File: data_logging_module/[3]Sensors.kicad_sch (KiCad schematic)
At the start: 4 parts, among them U3 BME280

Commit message: Initial scheme
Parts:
- added C301, C302, C303, C304: 100nF, Capacitor_SMD:C_0805_2012Metric, symbol Device:C
- added R301, R302, R303: 4k7R, Resistor_SMD:R_0805_2012Metric, symbol Device:R
- added R304, R305: 5k1R, Resistor_SMD:R_0805_2012Metric, symbol Device:R
- added U301: BME280, Package_LGA:Bosch_LGA-8_2.5x2.5mm_P0.65mm_ClockwisePinNumbering, symbol Sensor:BME280
- added U5: DS18B20, Package_TO_SOT_THT:TO-92_Inline, symbol Sensor_Temperature:DS18B20
- RLO300: renamed from R10; value LDR07 -> LDR
- renumbered C11 to C300, R11 to R300, U3 to U300
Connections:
- net +3.3V: now also U300.2 (CSB), U300.6 (VDDIO), C301.1, C303.1, R302.1, R303.1, R304.1, U301.6 (VDDIO); no longer RLO300.2
- net GND: now also U300.1 (GND), U300.7 (GND), C301.2, C302.2, C303.2, C304.2, R305.2, U301.1 (GND), U301.7 (GND), U5.1 (GND)
- net I2C_SDA: now reaches U300.3 (SDI)
- net I2C_SDA: now also R302.2
- net I2C_SCL: now reaches U300.4 (SCK)
- net I2C_SCL: now also R303.2
- net at U300.5 (SDO): now also R304.2, R305.1
- net +3.3VA: now reaches U300.8 (VDD)
- net +3.3VA: now also RLO300.2, C302.1, C304.1, R301.1, U301.8 (VDD), U5.3 (V_{DD})
- net LDR_IN renamed LDR
- new net BME280_SCB: U301.2 (CSB)
- new net BME280_SCK: U301.4 (SCK)
- new net BME280_SDI: U301.3 (SDI)
- new net BME280_SDO: U301.5 (SDO)
- new net DS18B20: R301.2, U5.2 (DQ)
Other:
- note added: "BME 280 I2C"
- note added: "BME 280 SPI"
- note added: "DS18B20"
- note added: "LRO"
- note added: "SDO: I2C address bit 0 GND: '0'; VDDIO: '1'"
- moved on the sheet: C300, R300, RLO300, U300

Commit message: BOM updates
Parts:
- C300: Manufacturer Part Number (none) -> CL10B104KB8NNNC
- C301, C302, C303, C304: footprint Capacitor_SMD:C_0805_2012Metric -> Capacitor_SMD:C_0603_1608Metric; Manufacturer Part Number (none) -> CL10B104KB8NNNC
- R300: Manufacturer Part Number (none) -> 0805W8F1002T5E
- R301, R302, R303: Manufacturer Part Number (none) -> 0805W8F4701T5E
- R304, R305: Manufacturer UNI-ROYAL(Uniroyal Elec) -> UNI-ROYAL(Uniroyal Elec); Manufacturer Part Number (none) -> 0805W8F5101T5E
- RLO300: Manufacturer Part Number (none) -> GL5528(10-20)
- U300, U301: Manufacturer (none) -> Bosch Sensortec; Manufacturer Part Number (none) -> BME280
- U5: Manufacturer (none) -> UMW(Youtai Semiconductor Co., Ltd.); Manufacturer Part Number (none) -> DS18B20(UMW)
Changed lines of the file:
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@@
 			)
 		)
-		(property "Footprint" "Capacitor_SMD:C_0805_2012Metric"
+		(property "Footprint" "Capacitor_SMD:C_0603_1608Metric"
 			(at 36.5252 96.52 0)
 			(effects
@@
 		)
 		(property "Manufacturer Product Number" "CL21A106KOQNNNE"
+			(at 35.56 92.71 0)
+			(effects
+				(font
+					(size 1.27 1.27)
+				)
+				(hide yes)
+			)
+		)
+		(property "Manufacturer Part Number" "CL10B104KB8NNNC"
 			(at 35.56 92.71 0)
 			(effects
@@
 			)
 		)
-		(property "Footprint" "Capacitor_SMD:C_0805_2012Metric"
+		(property "Footprint" "Capacitor_SMD:C_0603_1608Metric"
 			(at 157.1752 99.06 0)
 			(effects
@@
 		)
 		(property "Manufacturer Product Number" "CL21A106KOQNNNE"
+			(at 156.21 95.25 0)
+			(effects
+				(font
+					(size 1.27 1.27)
+				)
+				(hide yes)
+			)
+		)
+		(property "Manufacturer Part Number" "CL10B104KB8NNNC"
 			(at 156.21 95.25 0)
 			(effects
@@
 			)
 		)
-		(property "Footprint" "Capacitor_SMD:C_0805_2012Metric"
+		(property "Footprint" "Capacitor_SMD:C_0603_1608Metric"
 			(at 181.3052 97.79 0)
 			(effects
@@
 		)
 		(property "Manufacturer Product Number" "CL21A106KOQNNNE"
+			(at 180.34 93.98 0)
+			(effects
+				(font
+					(size 1.27 1.27)
+				)
+				(hide yes)
+			)
+		)
+		(property "Manufacturer Part Number" "CL10B104KB8NNNC"
 			(at 180.34 93.98 0)
 			(effects
@@
 		)
 		(property "Manufacturer Product Number" "0805W8F1002T5E"
+			(at 179.07 36.83 0)
+			(effects
+				(font
+					(size 1.27 1.27)
+				)
+				(hide yes)
+			)
+		)
+		(property "Manufacturer Part Number" "0805W8F4701T5E"
 			(at 179.07 36.83 0)
 			(effects
@@
 			)
 		)
-		(property "Manufacturer" "UNI-ROYAL(Uniroyal Elec)"
+		(property "Manufacturer" "UNI-ROYAL(Uniroyal Elec) "
 			(at 100.33 107.95 0)
 			(effects
@@
 		)
 		(property "Manufacturer Product Number" "0805W8F1002T5E"
+			(at 100.33 107.95 0)
+			(effects
+				(font
+					(size 1.27 1.27)
+				)
+				(hide yes)
+			)
+		)
+		(property "Manufacturer Part Number" "0805W8F5101T5E"
 			(at 100.33 107.95 0)
 			(effects
@@
 			)
 		)
+		(property "Manufacturer Part Number" "0805W8F1002T5E"
+			(at 64.77 41.91 0)
+			(effects
+				(font
+					(size 1.27 1.27)
+				)
+				(hide yes)
+			)
+		)
 		(pin "2"
 		)
@@
 			)
 		)
+		(property "Manufacturer Part Number" "0805W8F4701T5E"
+			(at 69.85 106.68 0)
+			(effects
+				(font
+					(size 1.27 1.27)
+				)
+				(hide yes)
+			)
+		)
 		(pin "2"
 		)
@@
 			)
 		)
+		(property "Manufacturer Part Number" "GL5528(10-20)"
+			(at 58.42 35.56 0)
+			(effects
+				(font
+					(size 1.27 1.27)
+				)
+				(hide yes)
+			)
+		)
 		(pin "1"
 		)
@@
 			)
 		)
+		(property "Manufacturer Part Number" "CL10B104KB8NNNC"
+			(at 74.93 41.91 0)
+			(effects
+				(font
+					(size 1.27 1.27)
+				)
+				(hide yes)
+			)
+		)
 		(pin "2"
 		)
@@
 		)
 		(property "Manufacturer Product Number" "0805W8F1002T5E"
+			(at 80.01 106.68 0)
+			(effects
+				(font
+					(size 1.27 1.27)
+				)
+				(hide yes)
+			)
+		)
+		(property "Manufacturer Part Number" "0805W8F4701T5E"
 			(at 80.01 106.68 0)
 			(effects
@@
 			)
 		)
+		(property "Manufacturer" "Bosch Sensortec"
+			(at 168.91 123.19 0)
+			(effects
+				(font
+					(size 1.27 1.27)
+				)
+				(hide yes)
+			)
+		)
+		(property "Manufacturer Part Number" "BME280"
+			(at 168.91 123.19 0)
+			(effects
+				(font
+					(size 1.27 1.27)
+				)
+				(hide yes)
+			)
+		)
 		(pin "2"
 		)
@@
 			)
 		)
-		(property "Manufacturer" "UNI-ROYAL(Uniroyal Elec)"
+		(property "Manufacturer" "UNI-ROYAL(Uniroyal Elec) "
 			(at 100.33 118.11 0)
 			(effects
@@
 		)
 		(property "Manufacturer Product Number" "0805W8F1002T5E"
+			(at 100.33 118.11 0)
+			(effects
+				(font
+					(size 1.27 1.27)
+				)
+				(hide yes)
+			)
+		)
+		(property "Manufacturer Part Number" "0805W8F5101T5E"
 			(at 100.33 118.11 0)
 			(effects
@@
 			)
 		)
+		(property "Manufacturer" "Bosch Sensortec"
+			(at 48.26 120.65 0)
+			(effects
+				(font
+					(size 1.27 1.27)
+				)
+				(hide yes)
+			)
+		)
+		(property "Manufacturer Part Number" "BME280"
+			(at 48.26 120.65 0)
+			(effects
+				(font
+					(size 1.27 1.27)
+				)
+				(hide yes)
+			)
+		)
 		(pin "2"
 		)
@@
 			)
 		)
+		(property "Manufacturer" "UMW(Youtai Semiconductor Co., Ltd.)"
+			(at 167.64 41.91 0)
+			(effects
+				(font
+					(size 1.27 1.27)
+				)
+				(hide yes)
+			)
+		)
+		(property "Manufacturer Part Number" "DS18B20(UMW)"
+			(at 167.64 41.91 0)
+			(effects
+				(font
+					(size 1.27 1.27)
+				)
+				(hide yes)
+			)
+		)
 		(pin "3"
 		)
@@
 			)
 		)
-		(property "Footprint" "Capacitor_SMD:C_0805_2012Metric"
+		(property "Footprint" "Capacitor_SMD:C_0603_1608Metric"
 			(at 60.6552 95.25 0)
 			(effects
@@
 			(at 59.69 91.44 0)
 			(effects
+				(font
+					(size 1.27 1.27)
+				)
+				(hide yes)
+			)
+		)
+		(property "Manufacturer Part Number" "CL10B104KB8NNNC"
+			(at 59.69 91.44 0)
+			(effects

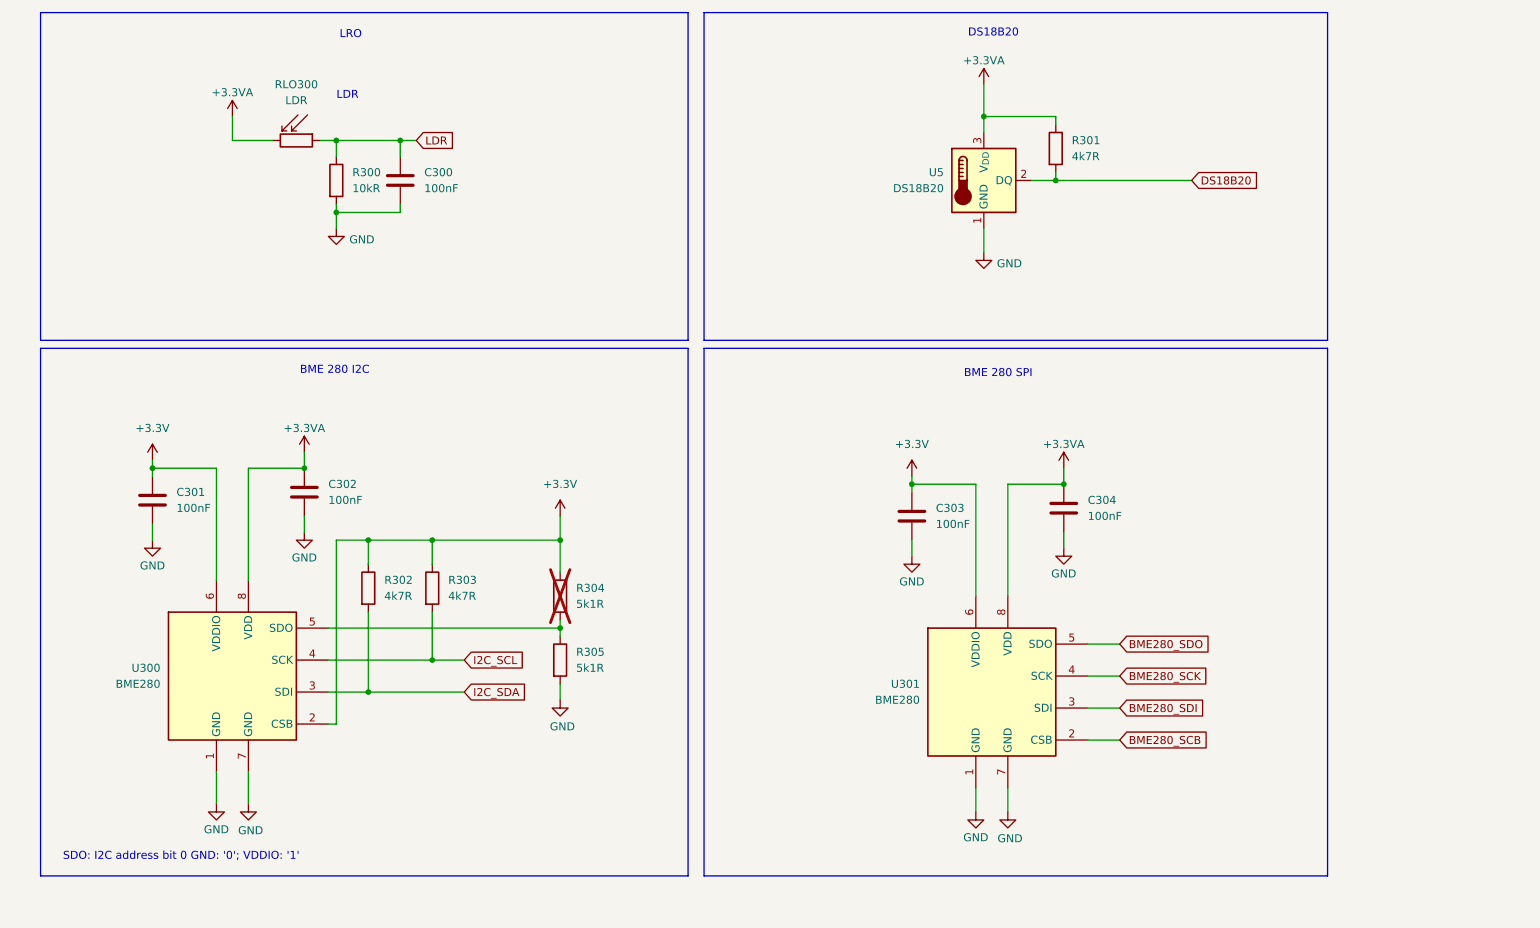
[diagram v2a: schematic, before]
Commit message: Add scheme plots
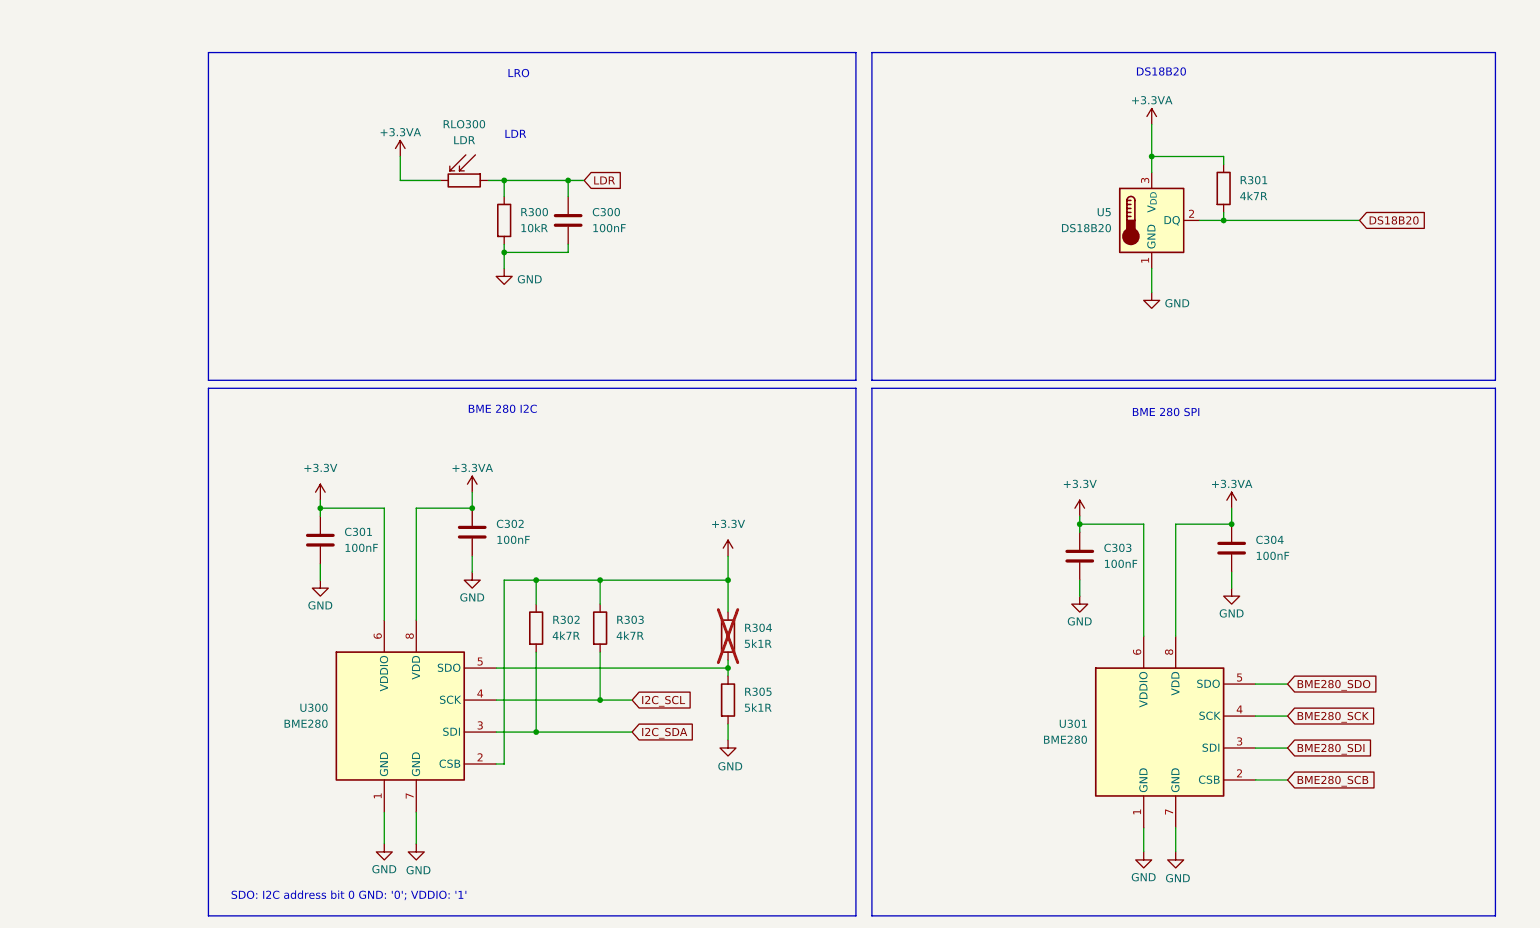
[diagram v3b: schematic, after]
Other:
- moved on the sheet: C300, C301, C302, C303, C304, R300, R301, R302, R303, R304, R305, RLO300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

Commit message: Add decoupling capacitors to analog sensors
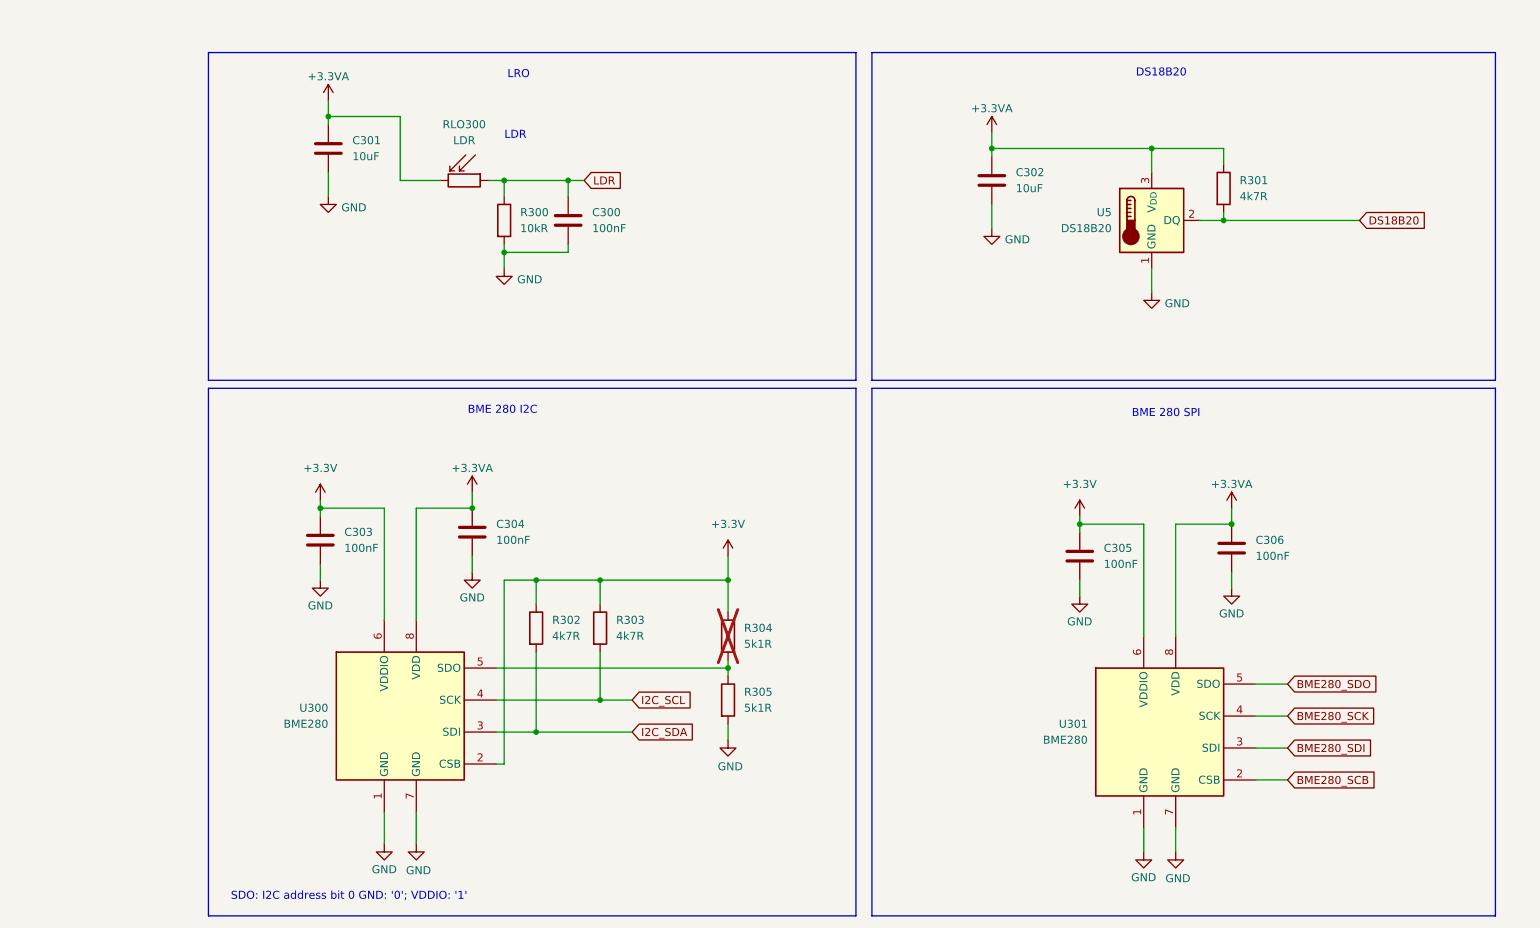
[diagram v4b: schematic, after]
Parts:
- added C301, C302: 10uF, Capacitor_SMD:C_0805_2012Metric, symbol Device:C
- renumbered C301 to C303, C302 to C304, C303 to C305, C304 to C306
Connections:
- net +3.3VA: now also C301.1, C302.1
- net GND: now also C301.2, C302.2
